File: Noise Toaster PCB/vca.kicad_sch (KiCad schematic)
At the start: 6 parts, among them Q7 2N5457, X12 Conn_01x01_Pin, X13 Conn_01x01_Pin

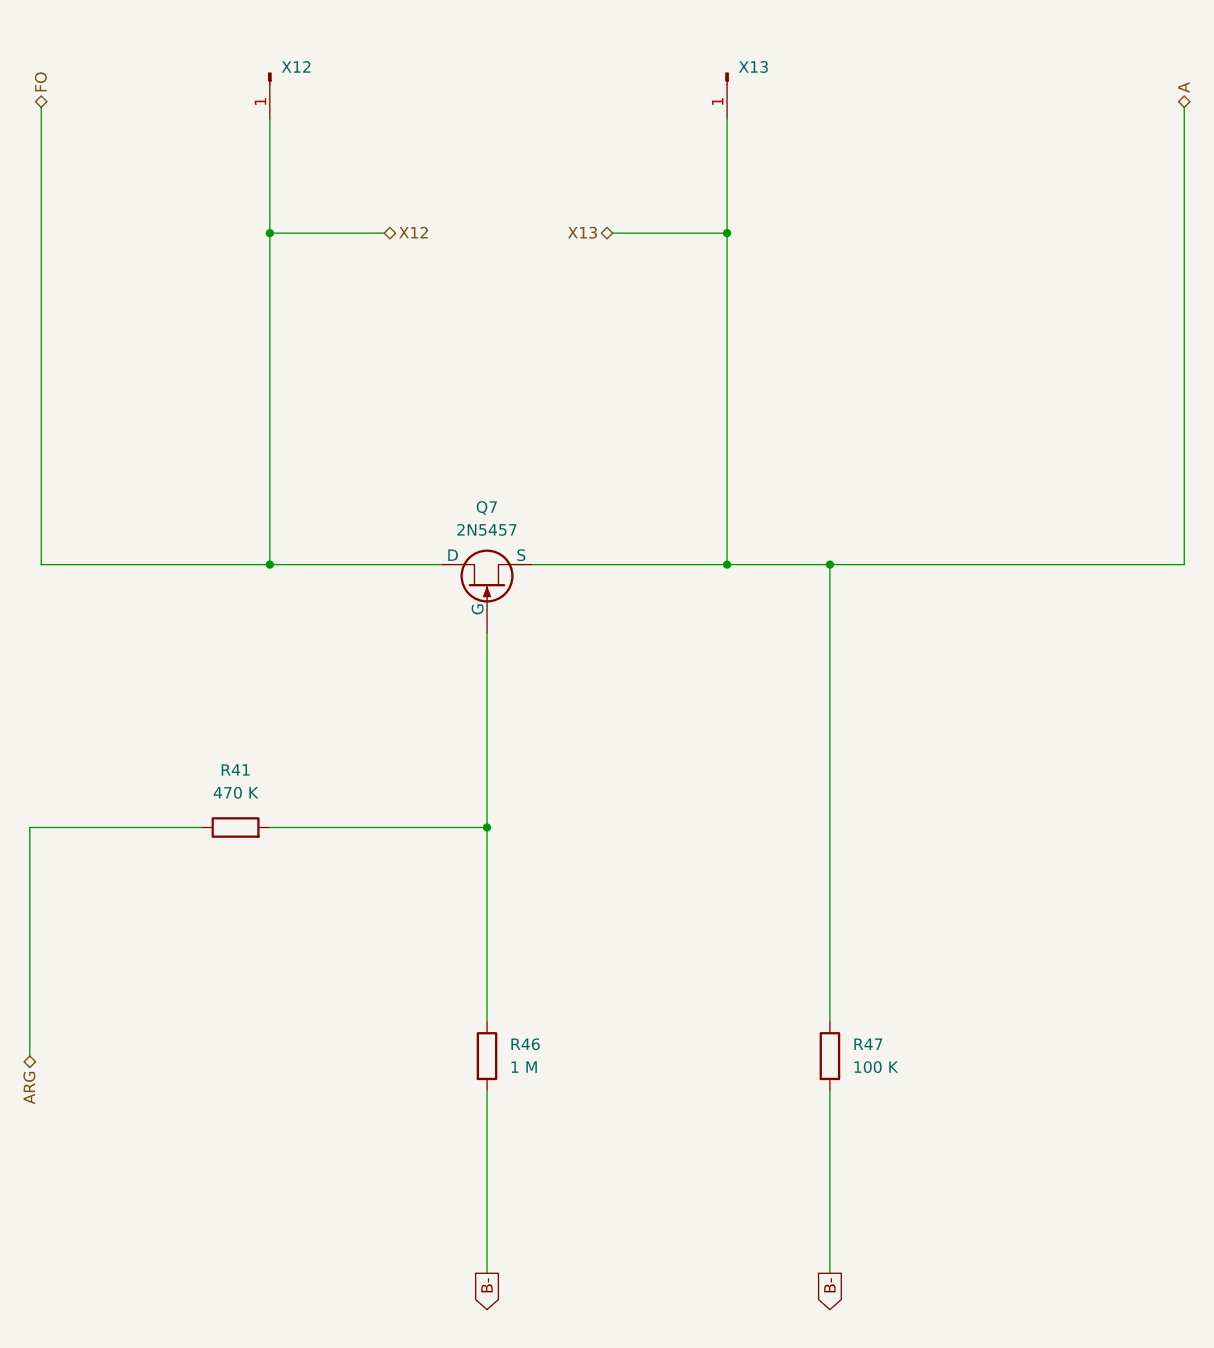
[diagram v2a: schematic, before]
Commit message: refactored schematics and added front panel
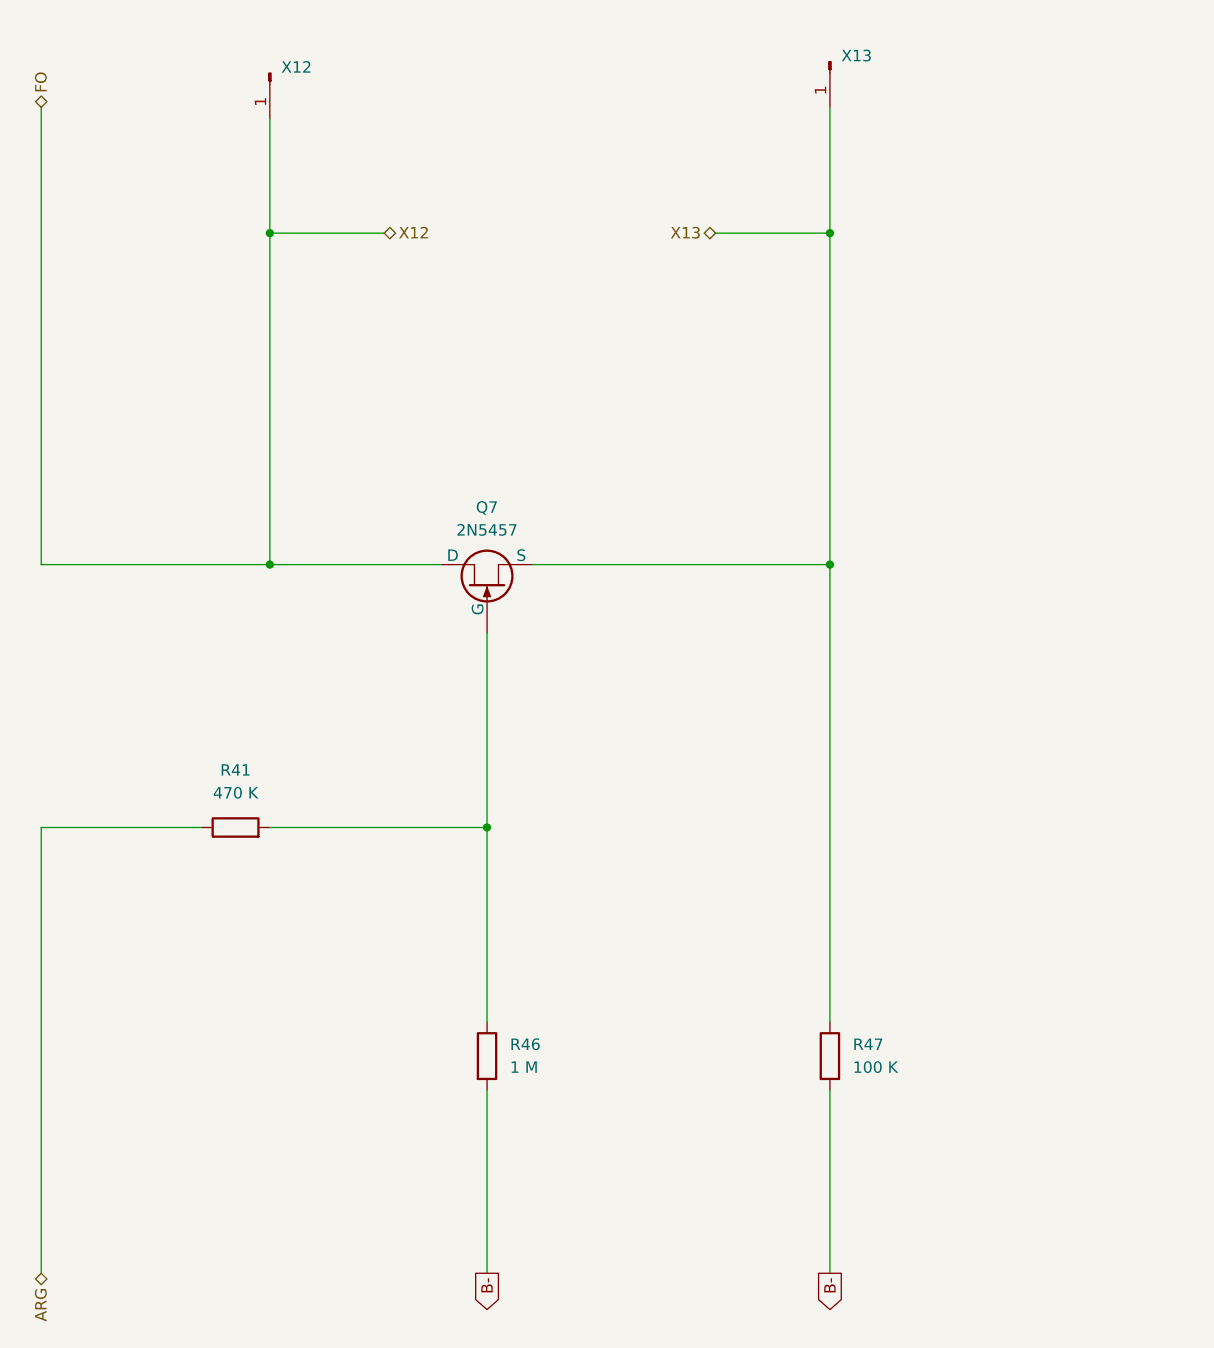
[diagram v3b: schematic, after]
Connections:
- net A renamed X13
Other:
- moved on the sheet: X13
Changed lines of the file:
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@@
     (comment 3 "Music From Outer Space LLC")
   )
-  (junction (at 139.7 50.8) (diameter 0) (color 0 0 0 0)
-  )
-  (junction (at 139.7 87.63) (diameter 0) (color 0 0 0 0)
+  (junction (at 151.13 50.8) (diameter 0) (color 0 0 0 0)
   )
   (junction (at 88.9 50.8) (diameter 0) (color 0 0 0 0)
@@
   (junction (at 113.03 116.84) (diameter 0) (color 0 0 0 0)
   )
-  (wire (pts (xy 139.7 50.8) (xy 139.7 87.63))
+  (wire (pts (xy 151.13 50.8) (xy 151.13 87.63))
     (stroke (width 0) (type default))
   )
-  (wire (pts (xy 127 50.8) (xy 139.7 50.8))
+  (wire (pts (xy 138.43 50.8) (xy 151.13 50.8))
     (stroke (width 0) (type default))
   )
@@
     (stroke (width 0) (type default))
   )
-  (wire (pts (xy 190.5 36.83) (xy 190.5 87.63))
-    (stroke (width 0) (type default))
-  )
   (wire (pts (xy 113.03 116.84) (xy 113.03 138.43))
     (stroke (width 0) (type default))
@@
     (stroke (width 0) (type default))
   )
-  (wire (pts (xy 81.28 116.84) (xy 62.23 116.84))
+  (wire (pts (xy 81.28 116.84) (xy 63.5 116.84))
     (stroke (width 0) (type default))
   )
@@
     (stroke (width 0) (type default))
   )
+  (wire (pts (xy 118.11 87.63) (xy 151.13 87.63))
+    (stroke (width 0) (type default))
+  )
   (wire (pts (xy 151.13 166.37) (xy 151.13 146.05))
     (stroke (width 0) (type default))
   )
-  (wire (pts (xy 62.23 116.84) (xy 62.23 142.24))
+  (wire (pts (xy 63.5 116.84) (xy 63.5 166.37))
     (stroke (width 0) (type default))
   )
-  (wire (pts (xy 139.7 38.1) (xy 139.7 50.8))
+  (wire (pts (xy 151.13 36.83) (xy 151.13 50.8))
     (stroke (width 0) (type default))
   )
   (wire (pts (xy 88.9 87.63) (xy 107.95 87.63))
-    (stroke (width 0) (type default))
-  )
-  (wire (pts (xy 190.5 87.63) (xy 151.13 87.63))
-    (stroke (width 0) (type default))
-  )
-  (wire (pts (xy 151.13 87.63) (xy 139.7 87.63))
     (stroke (width 0) (type default))
   )
@@
     (stroke (width 0) (type default))
   )
-  (wire (pts (xy 139.7 87.63) (xy 118.11 87.63))
-    (stroke (width 0) (type default))
-  )
   (global_label "B-" (shape output) (at 113.03 166.37 270) (fields_autoplaced)
     (effects (font (size 1.27 1.27)) (justify right))
@@
     )
   )
-  (hierarchical_label "X13" (shape bidirectional) (at 127 50.8 180) (fields_autoplaced)
+  (hierarchical_label "X13" (shape bidirectional) (at 138.43 50.8 180) (fields_autoplaced)
     (effects (font (size 1.27 1.27)) (justify right))
   )
-  (hierarchical_label "ARG" (shape bidirectional) (at 62.23 142.24 270) (fields_autoplaced)
+  (hierarchical_label "ARG" (shape bidirectional) (at 63.5 166.37 270) (fields_autoplaced)
     (effects (font (size 1.27 1.27)) (justify right))
   )
@@
   )
   (hierarchical_label "X12" (shape bidirectional) (at 101.6 50.8 0) (fields_autoplaced)
-    (effects (font (size 1.27 1.27)) (justify left))
-  )
-  (hierarchical_label "A" (shape bidirectional) (at 190.5 36.83 90) (fields_autoplaced)
     (effects (font (size 1.27 1.27)) (justify left))
   )
@@
     )
   )
-  (symbol (lib_id "Connector:Conn_01x01_Pin") (at 139.7 33.02 270) (unit 1)
+  (symbol (lib_id "Connector:Conn_01x01_Pin") (at 151.13 31.75 270) (unit 1)
     (in_bom yes) (on_board yes) (dnp no) (fields_autoplaced)
-    (property "Reference" "X13" (at 140.97 32.385 90)
+    (property "Reference" "X13" (at 152.4 31.115 90)
       (effects (font (size 1.27 1.27)) (justify left))
     )
-    (property "Value" "Conn_01x01_Pin" (at 140.97 34.925 90)
+    (property "Value" "Conn_01x01_Pin" (at 152.4 33.655 90)
       (effects (font (size 1.27 1.27)) (justify left) hide)
     )
-    (property "Footprint" "" (at 139.7 33.02 0)
+    (property "Footprint" "" (at 151.13 31.75 0)
       (effects (font (size 1.27 1.27)) hide)
     )
-    (property "Datasheet" "~" (at 139.7 33.02 0)
+    (property "Datasheet" "~" (at 151.13 31.75 0)
       (effects (font (size 1.27 1.27)) hide)
     )

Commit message: applied footprints
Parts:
- Q7: footprint (none) -> Package_TO_SOT_THT:TO-92_Inline
- R41, R46, R47: footprint (none) -> Resistor_THT:R_Axial_DIN0207_L6.3mm_D2.5mm_P10.16mm_Horizontal
- X12, X13: footprint (none) -> Connector_PinHeader_1.00mm:PinHeader_1x01_P1.00mm_Vertical
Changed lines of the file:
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@@
       (effects (font (size 1.27 1.27)))
     )
-    (property "Footprint" "" (at 110.49 85.09 0)
+    (property "Footprint" "Package_TO_SOT_THT:TO-92_Inline" (at 110.49 85.09 0)
       (effects (font (size 1.27 1.27)) hide)
     )
@@
       (effects (font (size 1.27 1.27)) (justify left))
     )
-    (property "Footprint" "" (at 149.352 142.24 90)
+    (property "Footprint" "Resistor_THT:R_Axial_DIN0207_L6.3mm_D2.5mm_P10.16mm_Horizontal" (at 149.352 142.24 90)
       (effects (font (size 1.27 1.27)) hide)
     )
@@
       (effects (font (size 1.27 1.27)) (justify left) hide)
     )
-    (property "Footprint" "" (at 151.13 31.75 0)
+    (property "Footprint" "Connector_PinHeader_1.00mm:PinHeader_1x01_P1.00mm_Vertical" (at 151.13 31.75 0)
       (effects (font (size 1.27 1.27)) hide)
     )
@@
       (effects (font (size 1.27 1.27)) (justify left) hide)
     )
-    (property "Footprint" "" (at 88.9 33.02 0)
+    (property "Footprint" "Connector_PinHeader_1.00mm:PinHeader_1x01_P1.00mm_Vertical" (at 88.9 33.02 0)
       (effects (font (size 1.27 1.27)) hide)
     )
@@
       (effects (font (size 1.27 1.27)) (justify left))
     )
-    (property "Footprint" "" (at 111.252 142.24 90)
+    (property "Footprint" "Resistor_THT:R_Axial_DIN0207_L6.3mm_D2.5mm_P10.16mm_Horizontal" (at 111.252 142.24 90)
       (effects (font (size 1.27 1.27)) hide)
     )
@@
       (effects (font (size 1.27 1.27)))
     )
-    (property "Footprint" "" (at 85.09 118.618 90)
+    (property "Footprint" "Resistor_THT:R_Axial_DIN0207_L6.3mm_D2.5mm_P10.16mm_Horizontal" (at 85.09 118.618 90)
       (effects (font (size 1.27 1.27)) hide)
     )

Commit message: placed pards of the pcb properly
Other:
- company: http://musicfromouterspace.com/analogsynth_new/NOISETOASTER/NOISETOASTER.php -> Music From Outer Space LLC
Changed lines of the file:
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@@
     (title "Coltage Contrlled Amplifier")
     (rev "0.5")
-    (company "http://musicfromouterspace.com/analogsynth_new/NOISETOASTER/NOISETOASTER.php")
+    (company "Music From Outer Space LLC")
     (comment 1 "Licence: CC-BY-NC-SA")
     (comment 2 "Original Design by Ray Wilson")
-    (comment 3 "Music From Outer Space LLC")
+    (comment 3 "http://musicfromouterspace.com/analogsynth_new/NOISETOASTER/NOISETOASTER.php")
   )
   (junction (at 151.13 50.8) (diameter 0) (color 0 0 0 0)

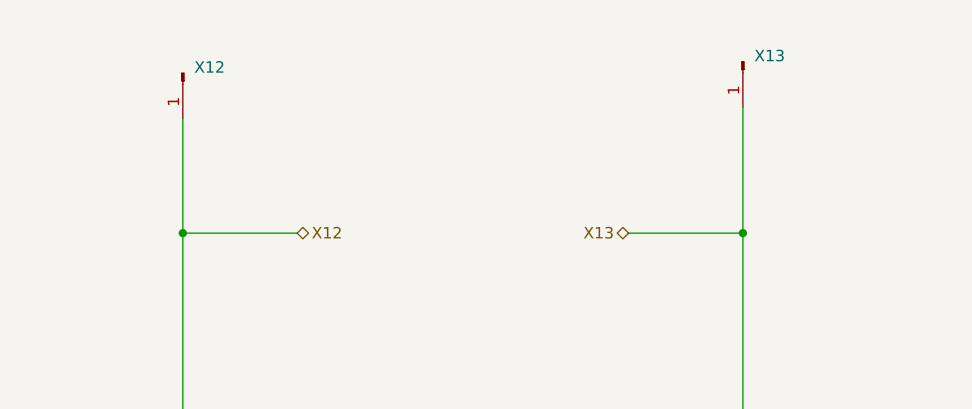
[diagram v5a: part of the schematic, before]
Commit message: changed header pins to groups
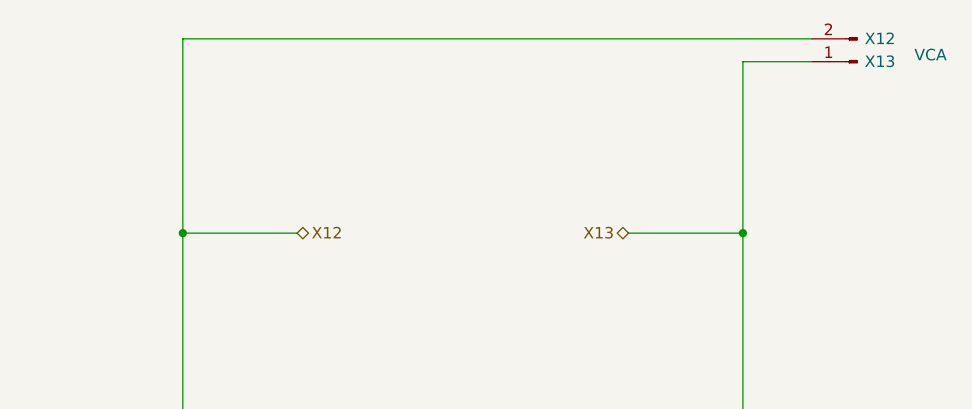
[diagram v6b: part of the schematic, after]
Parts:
- removed X12, X13: Conn_01x01_Pin, Connector_PinHeader_1.00mm:PinHeader_1x01_P1.00mm_Vertical, symbol Connector:Conn_01x01_Pin
- added J8: VCA, Connector_PinHeader_2.00mm:PinHeader_1x02_P2.00mm_Vertical, symbol Connector:Conn_01x02_Pin
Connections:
- net FO: now also J8.2 (Pin_2)
- net X13: now also J8.1 (Pin_1)
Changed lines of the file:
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@@
   (title_block
     (title "Coltage Contrlled Amplifier")
-    (rev "0.5")
+    (rev "0.6")
     (company "Music From Outer Space LLC")
     (comment 1 "Licence: CC-BY-NC-SA")
@@
     (stroke (width 0) (type default))
   )
+  (wire (pts (xy 151.13 31.75) (xy 158.75 31.75))
+    (stroke (width 0) (type default))
+  )
   (wire (pts (xy 88.9 50.8) (xy 101.6 50.8))
     (stroke (width 0) (type default))
@@
     (stroke (width 0) (type default))
   )
-  (wire (pts (xy 88.9 38.1) (xy 88.9 50.8))
+  (wire (pts (xy 88.9 29.21) (xy 88.9 50.8))
     (stroke (width 0) (type default))
   )
@@
     (stroke (width 0) (type default))
   )
-  (wire (pts (xy 151.13 36.83) (xy 151.13 50.8))
+  (wire (pts (xy 158.75 29.21) (xy 88.9 29.21))
+    (stroke (width 0) (type default))
+  )
+  (wire (pts (xy 151.13 31.75) (xy 151.13 50.8))
     (stroke (width 0) (type default))
   )
@@
     )
   )
+  (symbol (lib_id "Connector:Conn_01x02_Pin") (at 163.83 31.75 180) (unit 1)
+    (in_bom yes) (on_board yes) (dnp no)
+    (property "Reference" "J8" (at 165.1 29.21 0)
+      (effects (font (size 1.27 1.27)) (justify right) hide)
+    )
+    (property "Value" "VCA" (at 170.18 31.75 0)
+      (effects (font (size 1.27 1.27)) (justify right top))
+    )
+    (property "Footprint" "Connector_PinHeader_2.00mm:PinHeader_1x02_P2.00mm_Vertical" (at 163.83 31.75 0)
+      (effects (font (size 1.27 1.27)) hide)
+    )
+    (property "Datasheet" "~" (at 163.83 31.75 0)
+      (effects (font (size 1.27 1.27)) hide)
+    )
+    (property "X13" "X13" (at 166.37 31.75 0)
+      (effects (font (size 1.27 1.27)))
+    )
+    (property "X12" "X12" (at 166.37 29.21 0)
+      (effects (font (size 1.27 1.27)))
+    )
+    (pin "1")
+    (pin "2")
+    (instances
+      (project "Noise Toaster PCB"
+        (path "/7be3f398-d902-4566-9ee4-0bff072cd47e/6dd5f5bc-1b9c-4908-9997-3d64c0cf1aef"
+          (reference "J8") (unit 1)
+        )
+      )
+    )
+  )
   (symbol (lib_id "Device:R") (at 151.13 142.24 0) (unit 1)
     (in_bom yes) (on_board yes) (dnp no) (fields_autoplaced)
@@
         )
       )
-    )
-  )
-  (symbol (lib_id "Connector:Conn_01x01_Pin") (at 151.13 31.75 270) (unit 1)
-    (in_bom yes) (on_board yes) (dnp no) (fields_autoplaced)
-    (property "Reference" "X13" (at 152.4 31.115 90)
-      (effects (font (size 1.27 1.27)) (justify left))
-    )
-    (property "Value" "Conn_01x01_Pin" (at 152.4 33.655 90)
-      (effects (font (size 1.27 1.27)) (justify left) hide)
-    )
-    (property "Footprint" "Connector_PinHeader_1.00mm:PinHeader_1x01_P1.00mm_Vertical" (at 151.13 31.75 0)
-      (effects (font (size 1.27 1.27)) hide)
-    )
-    (property "Datasheet" "~" (at 151.13 31.75 0)
-      (effects (font (size 1.27 1.27)) hide)
-    )
-    (pin "1")
-    (instances
-      (project "Noise Toaster PCB"
-        (path "/7be3f398-d902-4566-9ee4-0bff072cd47e/6dd5f5bc-1b9c-4908-9997-3d64c0cf1aef"
-          (reference "X13") (unit 1)
-        )
-      )
-    )
-  )
-  (symbol (lib_id "Connector:Conn_01x01_Pin") (at 88.9 33.02 270) (unit 1)
-    (in_bom yes) (on_board yes) (dnp no) (fields_autoplaced)
-    (property "Reference" "X12" (at 90.17 32.385 90)
-      (effects (font (size 1.27 1.27)) (justify left))
-    )
-    (property "Value" "Conn_01x01_Pin" (at 90.17 34.925 90)
-      (effects (font (size 1.27 1.27)) (justify left) hide)
-    )
-    (property "Footprint" "Connector_PinHeader_1.00mm:PinHeader_1x01_P1.00mm_Vertical" (at 88.9 33.02 0)
-      (effects (font (size 1.27 1.27)) hide)
-    )
-    (property "Datasheet" "~" (at 88.9 33.02 0)
-      (effects (font (size 1.27 1.27)) hide)
-    )
-    (pin "1")
-    (instances
-      (project "Noise Toaster PCB"
-        (path "/7be3f398-d902-4566-9ee4-0bff072cd47e/6dd5f5bc-1b9c-4908-9997-3d64c0cf1aef"
-          (reference "X12") (unit 1)
-        )
-      )
